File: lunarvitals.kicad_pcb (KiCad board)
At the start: 2 copper layers, 49.5 x 35 mm, 41 parts, among them J1 ConductiveCord, J2 MPU6050, J3 SEN11574, J5 USB_C_Receptacle_PowerOnly_6P, J6 Battery, Q1 FS8205A, U1 NRF52840-DONGLE, U2 BMP280, U3 AP2112K-3.3, U4 TP4056, U5 MLX90614ESF-AAA-000-TU, U6 DW01A

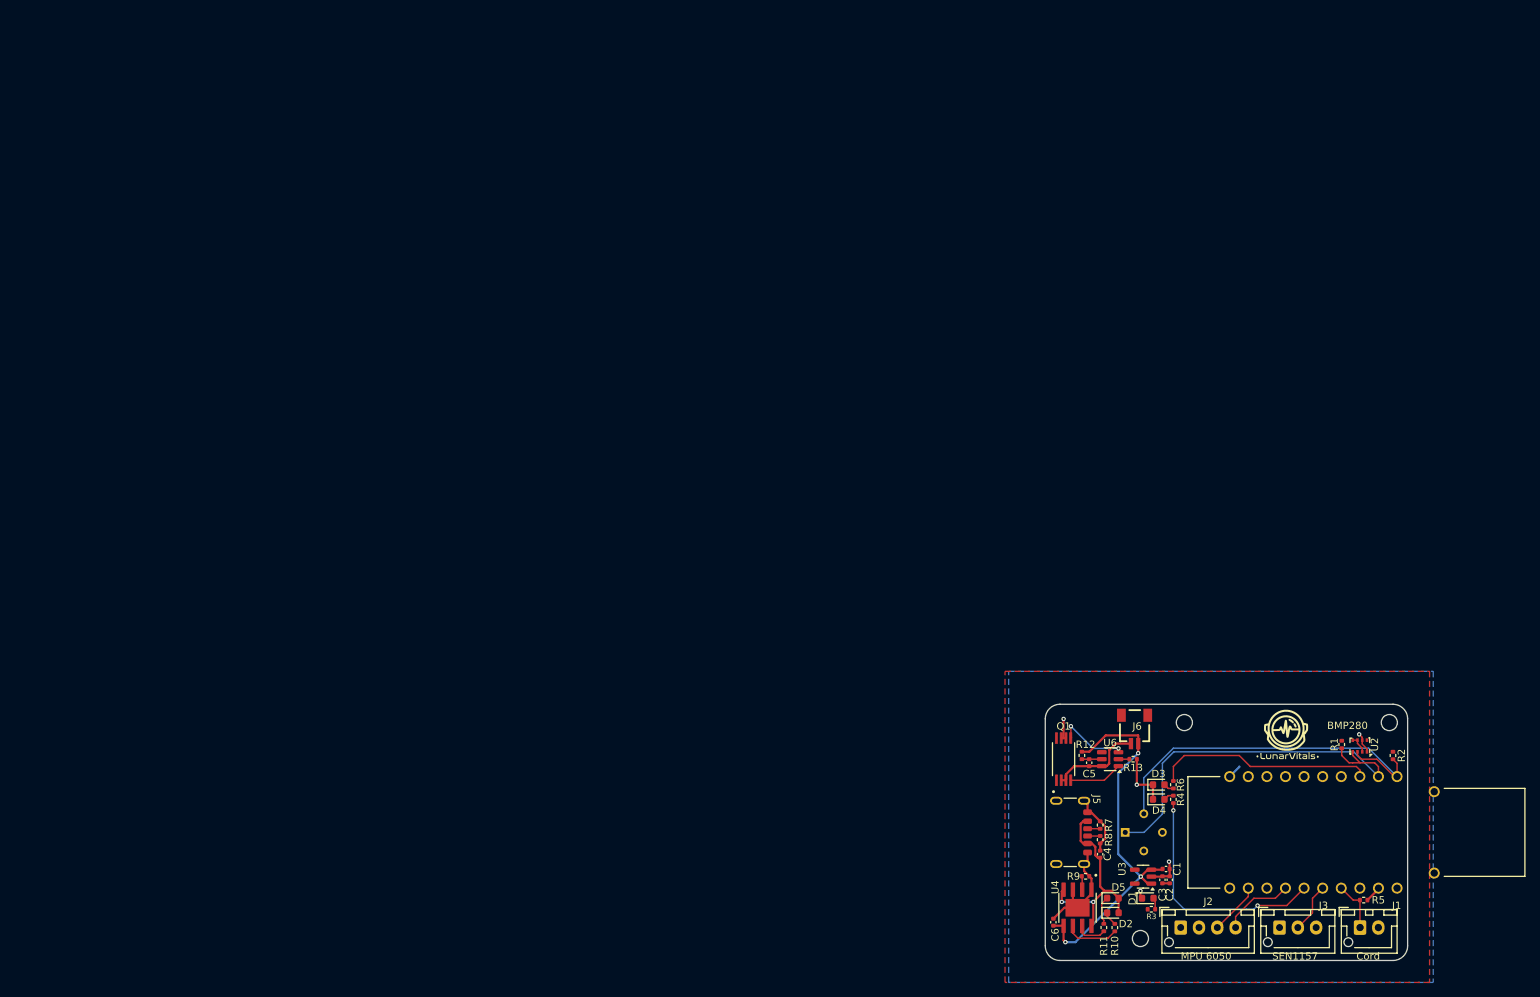
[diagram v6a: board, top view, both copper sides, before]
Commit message: pcb updates (logo, conductive cord, charging diodes, layout)
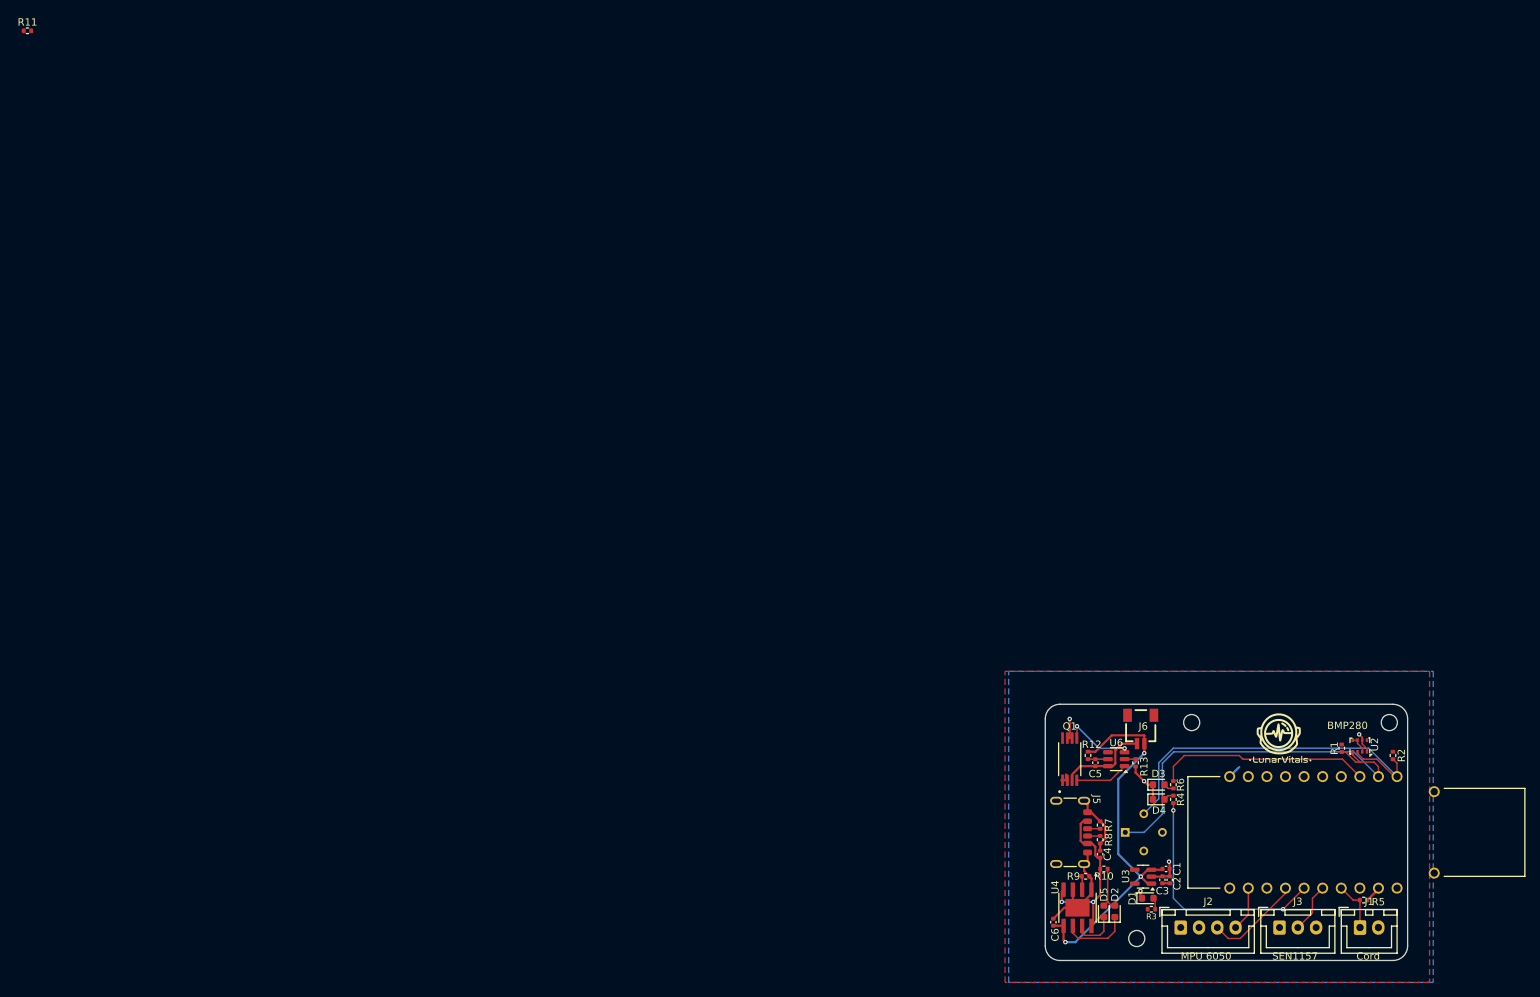
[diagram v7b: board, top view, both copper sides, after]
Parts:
- removed the G*** at (166.0, 110.5)
- added G***: LOGO, lunar_vitals_custom:lunarvitals_logo_bigger, B.Cu at (165.5, 109.5)
- J1: footprint Connector_JST:JST_XH_B2B-XH-AM_1x02_P2.50mm_Vertical -> Connector_JST:JST_XH_B2B-XH-A_1x02_P2.50mm_Vertical
- J2: footprint Connector_JST:JST_XH_B4B-XH-AM_1x04_P2.50mm_Vertical -> Connector_JST:JST_XH_B4B-XH-A_1x04_P2.50mm_Vertical
- J3: footprint Connector_JST:JST_XH_B3B-XH-AM_1x03_P2.50mm_Vertical -> Connector_JST:JST_XH_B3B-XH-A_1x03_P2.50mm_Vertical
- moved R11 191.4 mm to (0.95, 0.49), turned to 0 degrees
- moved R10 8.15 mm to (148.0, 115.0), turned to 0 degrees
- moved D5 1.82 mm to (149.5, 120.8), turned to 90 degrees
- moved D2 1.25 mm to (148.0, 120.8), turned to 90 degrees
- moved G*** 1.12 mm to (172.0, 97.0)
- moved H1 1.00 mm to (160.0, 95.0)
- moved C5 0.84 mm to (146.8, 100.5)
- moved J6 0.84 mm to (153.0, 95.9)
- moved Q1 0.84 mm to (143.3, 100.0)
- moved R12 0.84 mm to (145.8, 99.5)
- moved U6 0.84 mm to (149.7, 100.0)
- moved R13 0.60 mm to (152.3, 100.5), turned to 90 degrees
- moved R1 0.51 mm to (180.5, 98.5)
- moved H3 0.50 mm to (152.5, 124.5)
- turned R5 to 180 degrees
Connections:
- D2 pad 2: +5V -> Net-(D2-A)
- D5 pad 2: +5V -> Net-(D2-A)
- J1 pad 2: +3.3V -> GND
- J2 pad 3: /I2C1_SDA -> /I2C1_SCL
- J2 pad 4: /I2C1_SCL -> /I2C1_SDA
- R10 pad 1: Net-(U4-~{STDBY}) -> +5V
- R10 pad 2: Net-(D2-K) -> Net-(D2-A)
- R11 pad 1: Net-(U4-~{CHRG}) -> unconnected-(R11-Pad1)
- R11 pad 2: Net-(D5-K) -> unconnected-(R11-Pad2)
- R5 pad 1: /AIN7 -> +3.3V
- R5 pad 2: +3.3V -> /AIN7
- U4 pad 6: Net-(U4-~{STDBY}) -> Net-(D5-K)
- U4 pad 7: Net-(U4-~{CHRG}) -> Net-(D2-K)
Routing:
- net Net-(U4-~{STDBY}): track 7.39 -> 0.00 mm
- net Net-(D2-A): track 0.00 -> 6.41 mm
- net Net-(D5-K): track 3.93 -> 9.34 mm
- net +5V: track 29.1 -> 24.3 mm
- net Net-(U4-~{CHRG}): track 4.30 -> 0.00 mm
- net Net-(D2-K): track 1.95 -> 6.23 mm
- net /I2C1_SCL: track 9.92 -> 13.2 mm
- net GND: track 46.1 -> 44.2 mm
- net /I2C1_SDA: track 7.13 -> 6.10 mm
- net /I2C0_SCL: track 54.7 -> 53.8 mm
- net /GPIO17: track 29.8 -> 29.3 mm

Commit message: fixed out of stock fs8205 and other small fixes
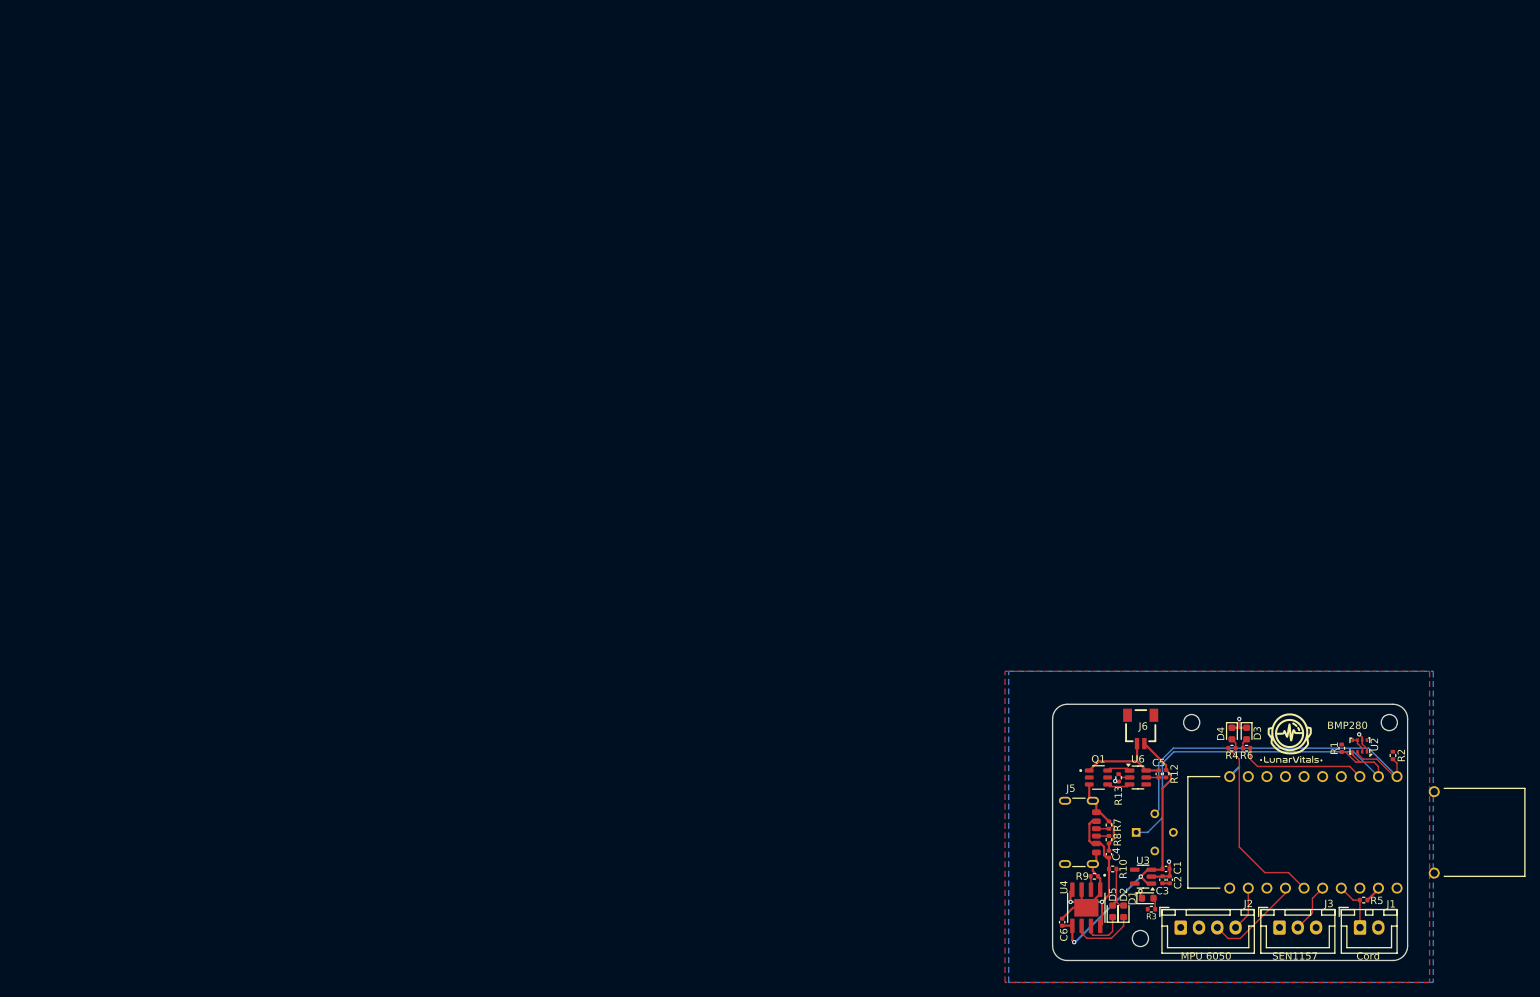
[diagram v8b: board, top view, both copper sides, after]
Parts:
- removed R11: 1k, Resistor_SMD:R_0402_1005Metric
- Q1: value FS8205A -> FS8205; footprint FS8205A:SOP65P640X120-8N -> FS8205A:SOT95P280X145-6N
- moved D3 13.9 mm to (167.5, 96.5), turned to -90 degrees
- moved D4 13.4 mm to (165.5, 96.5), turned to -90 degrees
- moved R6 11.2 mm to (167.5, 98.5), turned to 180 degrees
- moved R12 11.0 mm to (156.5, 102.0)
- moved R4 10.6 mm to (165.5, 98.5), turned to 0 degrees
- moved C5 8.80 mm to (155.5, 102.0), turned to 90 degrees
- moved Q1 4.66 mm to (147.3, 102.5), turned to 0 degrees
- moved U6 3.87 mm to (152.7, 102.5), turned to 0 degrees
- moved R13 3.09 mm to (150.0, 102.5)
- moved G*** 1.50 mm to (173.5, 97.0)
- moved U5 1.50 mm to (155.0, 110.0)
- moved C6 1.20 mm to (142.3, 122.3)
- moved R10 1.20 mm to (149.2, 115.0)
- moved R9 1.20 mm to (146.7, 116.0)
- moved C4 1.20 mm to (148.7, 113.0)
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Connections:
- Q1 pad 1: unconnected-(Q1-Pad1)_1 -> /B-
- Q1 pad 2: /B- -> unconnected-(Q1-Pad2)_1
- Q1 pad 3: /B- -> GND
- Q1 pad 4: Net-(U6-OD) -> Net-(U6-OC)
- Q1 pad 5: Net-(U6-OC) -> unconnected-(Q1-Pad2)
- Q1 pad 6: GND -> Net-(U6-OD)
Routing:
- net BOut+: track 53.7 -> 40.9 mm, vias 3 -> 2
- net /GPIO17: track 29.3 -> 17.5 mm
- net /GPIO2: track 32.7 -> 25.3 mm, vias 2 -> 0
- net Net-(U6-OC): track 10.1 -> 3.24 mm, vias 2 -> 0
- net Net-(U6-OD): track 7.32 -> 3.24 mm
- net GND: track 44.2 -> 41.2 mm
- net /I2C0_SCL: track 53.8 -> 52.6 mm
- net /I2C0_SDA: track 52.3 -> 51.7 mm
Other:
- board size 49.5 x 35 mm -> 48.5 x 35 mm
